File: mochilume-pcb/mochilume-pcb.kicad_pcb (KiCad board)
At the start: 2 copper layers, 47.9 x 76.8 mm, 16 parts

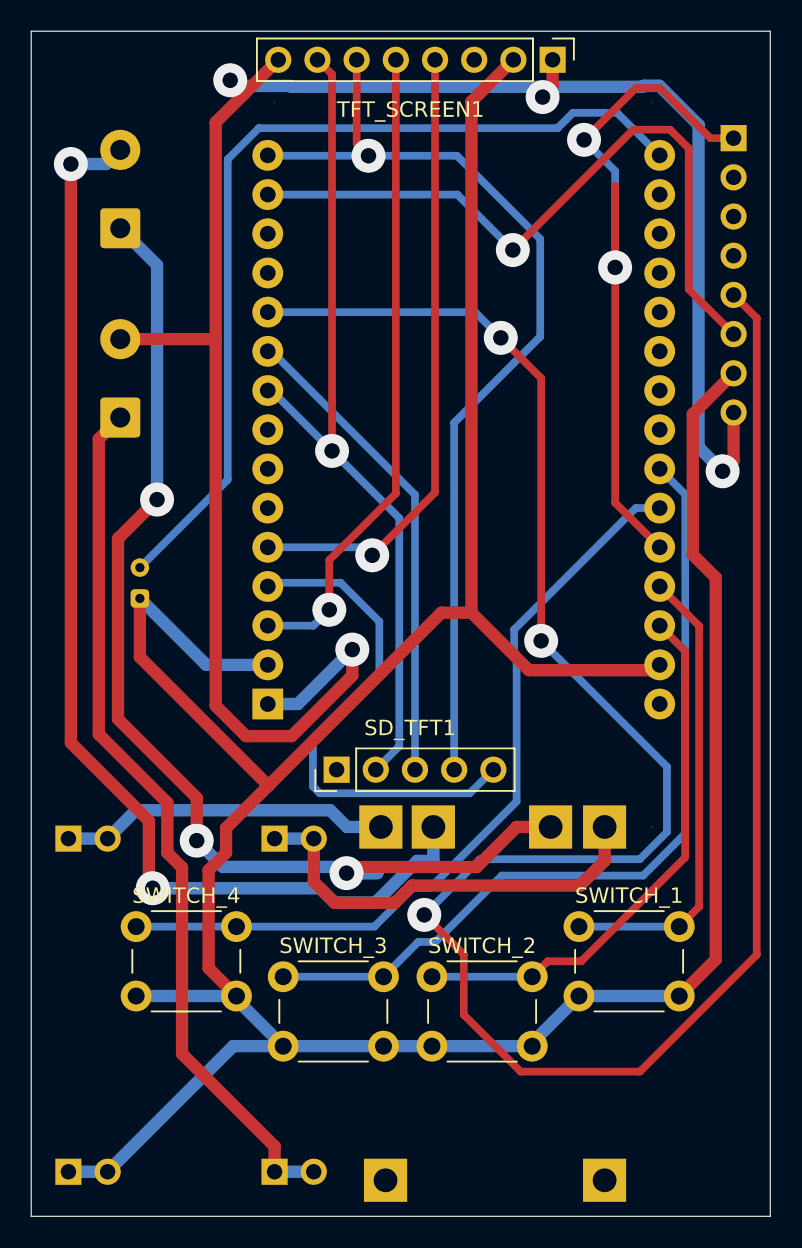
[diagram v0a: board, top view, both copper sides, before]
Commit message: update pcb: remove sd card tracks
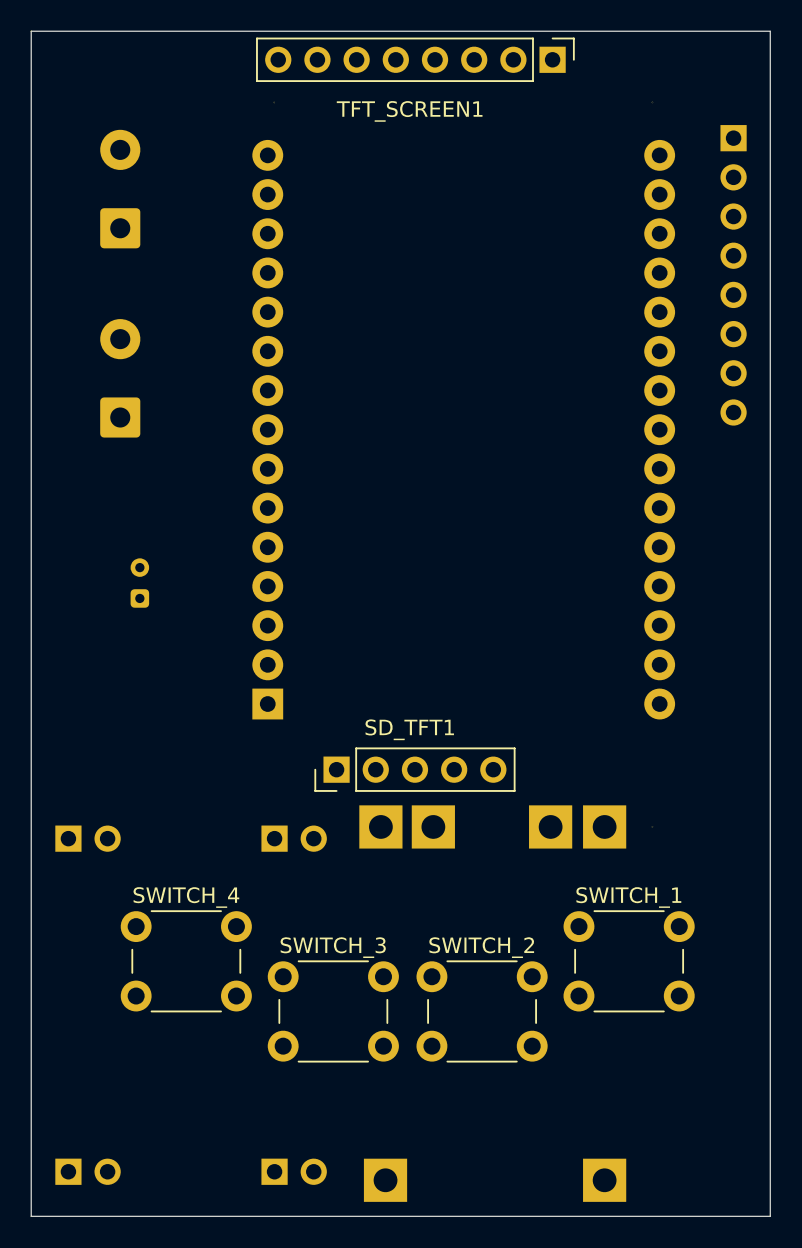
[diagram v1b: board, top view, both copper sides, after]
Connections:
- ESP32-WROOM-DEVKIT-V1 pad 10: SD_MISO -> unconnected-(ESP32-WROOM-DEVKIT-V1-D19-Pad10)
- ESP32-WROOM-DEVKIT-V1 pad 15: SD_MOSI -> TFT_SDA
- ESP32-WROOM-DEVKIT-V1 pad 4: SD_CS -> unconnected-(ESP32-WROOM-DEVKIT-V1-D2-Pad4)
- ESP32-WROOM-DEVKIT-V1 pad 9: SD_SCK -> TFT_SCK
- SD_TFT1 pad 1: SD_CD -> unconnected-(SD_TFT1-Pin_1-Pad1)
- SD_TFT1 pad 2: SD_SCK -> unconnected-(SD_TFT1-Pin_2-Pad2)
- SD_TFT1 pad 3: SD_MISO -> unconnected-(SD_TFT1-Pin_3-Pad3)
- SD_TFT1 pad 4: SD_MOSI -> unconnected-(SD_TFT1-Pin_4-Pad4)
- SD_TFT1 pad 5: SD_CS -> unconnected-(SD_TFT1-Pin_5-Pad5)
- TFT_SCREEN1 pad 6: SD_MOSI -> TFT_SDA
- TFT_SCREEN1 pad 7: SD_SCK -> TFT_SCK
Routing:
- net GND: track 208.8 -> 0.00 mm
- net AC_SDA: track 144.8 -> 0.00 mm, vias 3 -> 0
- net VCC: track 133.1 -> 0.00 mm, vias 4 -> 0
- net BATTERY -: track 74.6 -> 0.00 mm, vias 2 -> 0
- net BATTERY +: track 72.9 -> 0.00 mm, vias 3 -> 0
- net SD_MOSI: track 63.1 -> 0.00 mm, vias 1 -> 0
- net AC_TRIG: track 62.0 -> 0.00 mm, vias 2 -> 0
- net Net-(ESP32-WROOM-DEVKIT-V1-EN): track 59.2 -> 0.00 mm
- net VCC_IN: track 56.7 -> 0.00 mm
- net SD_SCK: track 54.6 -> 0.00 mm, vias 1 -> 0
- net SW_3: track 54.2 -> 0.00 mm
- net SW_4: track 51.9 -> 0.00 mm
- net AC_SCL: track 45.8 -> 0.00 mm, vias 1 -> 0
- net TFT_A0: track 41.8 -> 0.00 mm, vias 1 -> 0
- net TFT_RES: track 40.8 -> 0.00 mm, vias 1 -> 0
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
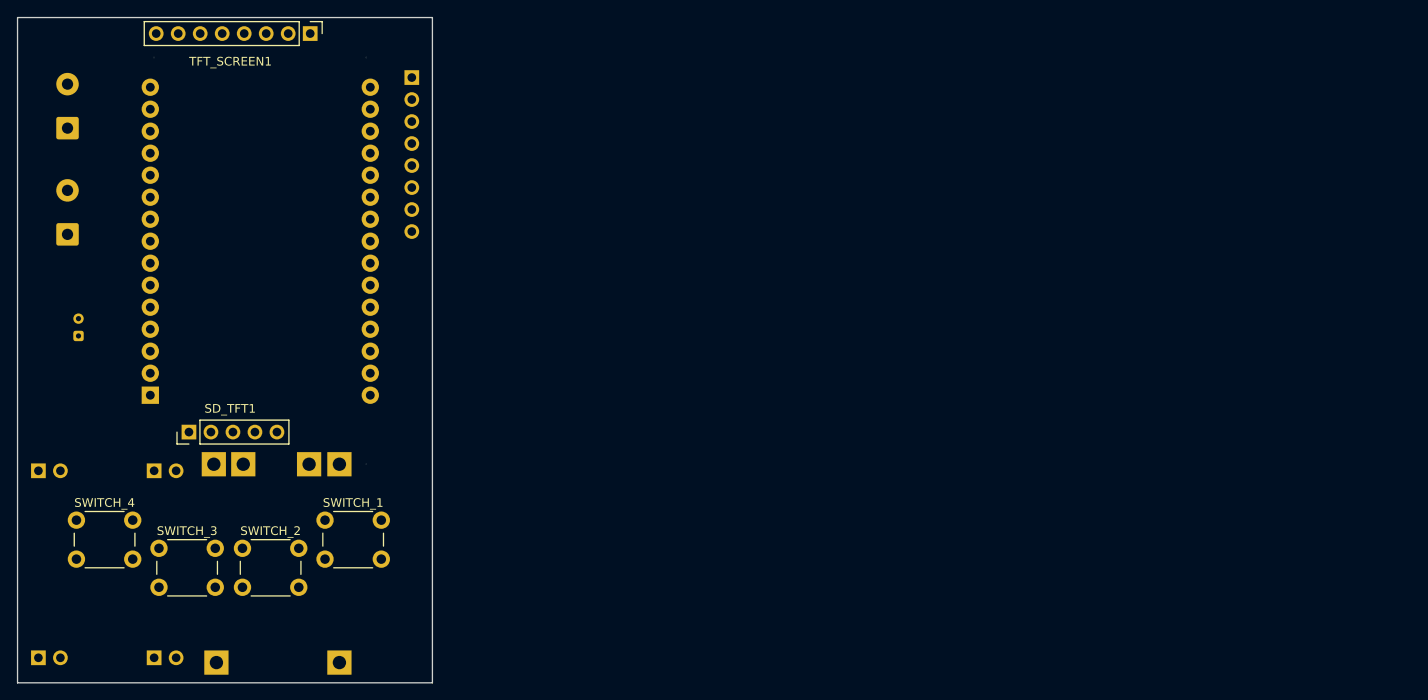
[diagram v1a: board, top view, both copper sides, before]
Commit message: fix pcb: update footprints and add pcb sketch without vias
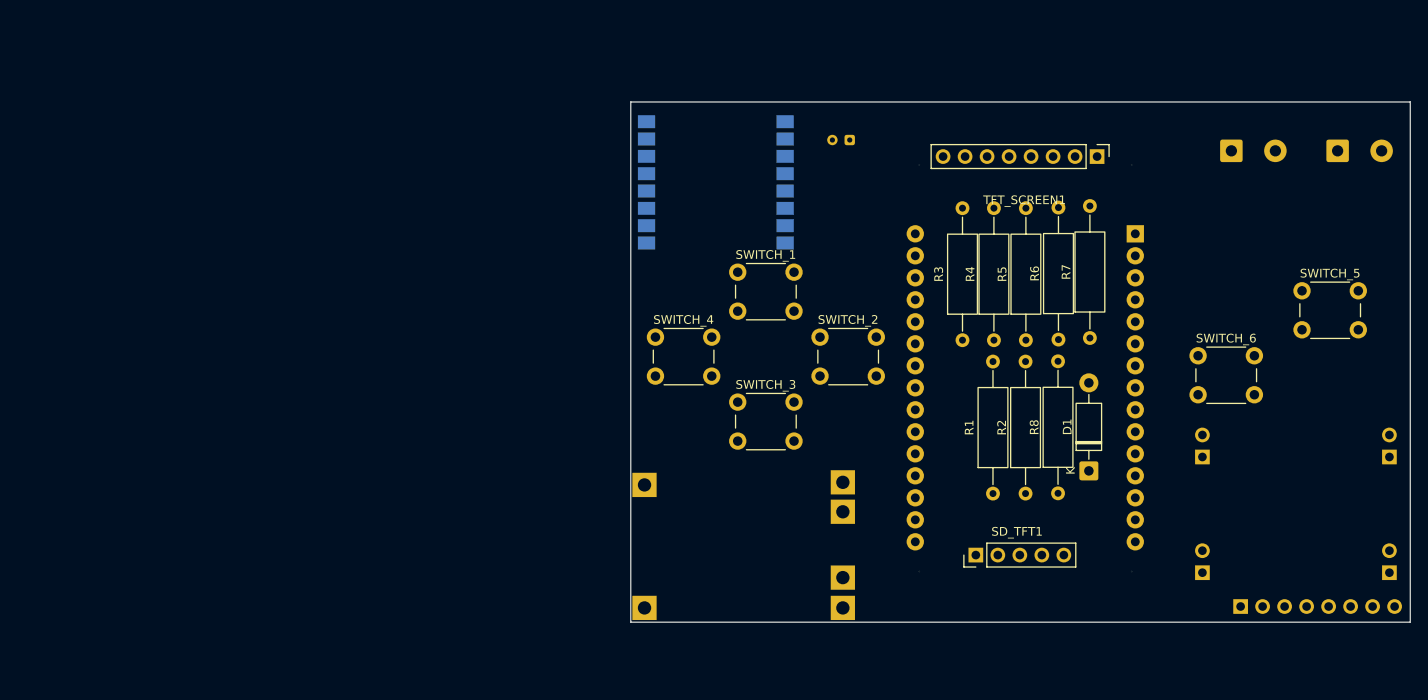
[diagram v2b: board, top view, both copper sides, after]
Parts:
- added D1: 1N5819, Diode_THT:D_DO-41_SOD81_P10.16mm_Horizontal, F.Cu at (225.9, 125.3)
- added R1: 10K, Resistor_THT:R_Axial_DIN0309_L9.0mm_D3.2mm_P15.24mm_Horizontal, F.Cu at (214.8, 127.9)
- added R2: 10K, Resistor_THT:R_Axial_DIN0309_L9.0mm_D3.2mm_P15.24mm_Horizontal, F.Cu at (218.6, 127.9)
- added R3: 10K, Resistor_THT:R_Axial_DIN0309_L9.0mm_D3.2mm_P15.24mm_Horizontal, F.Cu at (211.3, 110.2)
- added R4: 10K, Resistor_THT:R_Axial_DIN0309_L9.0mm_D3.2mm_P15.24mm_Horizontal, F.Cu at (214.9, 110.2)
- added R5: 10K, Resistor_THT:R_Axial_DIN0309_L9.0mm_D3.2mm_P15.24mm_Horizontal, F.Cu at (218.6, 110.2)
- added R6: 10K, Resistor_THT:R_Axial_DIN0309_L9.0mm_D3.2mm_P15.24mm_Horizontal, F.Cu at (222.4, 110.1)
- added R7: 10K, Resistor_THT:R_Axial_DIN0309_L9.0mm_D3.2mm_P15.24mm_Horizontal, F.Cu at (226.0, 110.0)
- added R8: 10K, Resistor_THT:R_Axial_DIN0309_L9.0mm_D3.2mm_P15.24mm_Horizontal, F.Cu at (222.3, 127.9)
- added SWITCH_5: ~, Button_Switch_THT:SW_PUSH_6mm, F.Cu at (250.5, 104.5)
- added SWITCH_6: ~, Button_Switch_THT:SW_PUSH_6mm, F.Cu at (238.5, 112.0)
- added U1: llcc68_custom_module, RF_Module:Ai-Thinker-Ra-01-LoRa, B.Cu at (182.8, 92.0)
- moved GND1 156.3 mm to (260.6, 137.0), turned to 0 degrees
- moved BATTERRY_BORN1 146.7 mm to (254.6, 88.3), turned to 0 degrees
- moved VOUT1 144.5 mm to (260.6, 123.7), turned to 0 degrees
- moved GNDIN1 134.9 mm to (239.0, 137.0), turned to 0 degrees
- moved ON/OFF1 134.7 mm to (242.3, 88.3), turned to 0 degrees
- moved VIN1 121.0 mm to (239.0, 123.7), turned to 0 degrees
- moved ACCELEROMETER1 113.5 mm to (243.4, 140.9), turned to -90 degrees
- moved SD_TFT1 92.0 mm to (212.8, 135.0)
- moved TFT_SCREEN1 92.0 mm to (226.8, 89.0)
- moved C1 91.9 mm to (198.3, 87.1), turned to 180 degrees
- moved ESP32-WROOM-DEVKIT-V1 89.2 mm to (218.6, 113.4), turned to 180 degrees
- moved SWITCH_2 71.0 mm to (194.8, 109.8)
- moved SWITCH_4 70.1 mm to (175.8, 109.8)
- moved SWITCH_3 68.9 mm to (185.3, 117.3)
- moved SWITCH_1 55.6 mm to (185.3, 102.3)
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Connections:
- BATTERRY_BORN1 pad 2: BATTERY - -> GND
- ESP32-WROOM-DEVKIT-V1 pad 10: unconnected-(ESP32-WROOM-DEVKIT-V1-D19-Pad10) -> AC_TRIG
- ESP32-WROOM-DEVKIT-V1 pad 17: unconnected-(ESP32-WROOM-DEVKIT-V1-VP-Pad17) -> BATERIA
- ESP32-WROOM-DEVKIT-V1 pad 19: unconnected-(ESP32-WROOM-DEVKIT-V1-D34-Pad19) -> LORA_BUSY
- ESP32-WROOM-DEVKIT-V1 pad 20: unconnected-(ESP32-WROOM-DEVKIT-V1-D35-Pad20) -> SW_4
- ESP32-WROOM-DEVKIT-V1 pad 21: unconnected-(ESP32-WROOM-DEVKIT-V1-D32-Pad21) -> LORA_RST
- ESP32-WROOM-DEVKIT-V1 pad 22: unconnected-(ESP32-WROOM-DEVKIT-V1-D33-Pad22) -> LORA_DIO1
- ESP32-WROOM-DEVKIT-V1 pad 23: unconnected-(ESP32-WROOM-DEVKIT-V1-D25-Pad23) -> SW_3
- ESP32-WROOM-DEVKIT-V1 pad 24: SW_3 -> SW_1
- ESP32-WROOM-DEVKIT-V1 pad 25: SW_4 -> SW_2
- ESP32-WROOM-DEVKIT-V1 pad 26: AC_TRIG -> LORA_SCK
- ESP32-WROOM-DEVKIT-V1 pad 27: SW_1 -> LORA_MISO
- ESP32-WROOM-DEVKIT-V1 pad 28: SW_2 -> LORA_MOSI
- ESP32-WROOM-DEVKIT-V1 pad 30: unconnected-(ESP32-WROOM-DEVKIT-V1-VIN-Pad30) -> ESP_VIN
- ESP32-WROOM-DEVKIT-V1 pad 4: unconnected-(ESP32-WROOM-DEVKIT-V1-D2-Pad4) -> LORA_CS
- ESP32-WROOM-DEVKIT-V1 pad 6: unconnected-(ESP32-WROOM-DEVKIT-V1-RX2-Pad6) -> SW_6
- ESP32-WROOM-DEVKIT-V1 pad 7: unconnected-(ESP32-WROOM-DEVKIT-V1-TX2-Pad7) -> SW_5
- GNDIN1 pad 1: GNDIN -> GND
- GNDIN1 pad 2: GNDIN -> GND
- SWITCH_1 pad 1: SW_1 -> VCC
- SWITCH_1 pad 2: GND -> SW_1
- SWITCH_2 pad 1: SW_2 -> VCC
- SWITCH_2 pad 2: GND -> SW_2
- SWITCH_3 pad 1: SW_3 -> VCC
- SWITCH_3 pad 2: GND -> SW_3
- SWITCH_4 pad 1: SW_4 -> VCC
- SWITCH_4 pad 2: GND -> SW_4
- TP1 pad 1: unconnected-(TP1-VIN-Pad1) -> ESP_VIN
- TP1 pad 2: unconnected-(TP1-GNDIN-Pad2) -> GND
- TP1 pad 4: GNDIN -> GND
- TP1 pad 5: BATTERY + -> Net-(D1-K)
- TP1 pad 6: BATTERY - -> GND
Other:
- board size 47.9 x 76.8 mm -> 90 x 60.1 mm
